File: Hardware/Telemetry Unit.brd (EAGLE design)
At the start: 50.8 x 82.5 mm, 56 parts, among them IC1 MEGA128-A, IC2 FT232RL, J2 503182-1852, J3 10118193-0001LF, Q1 10MHz, U1 MPL3115A2, U2 AOZ1280, U3 ICM-20649

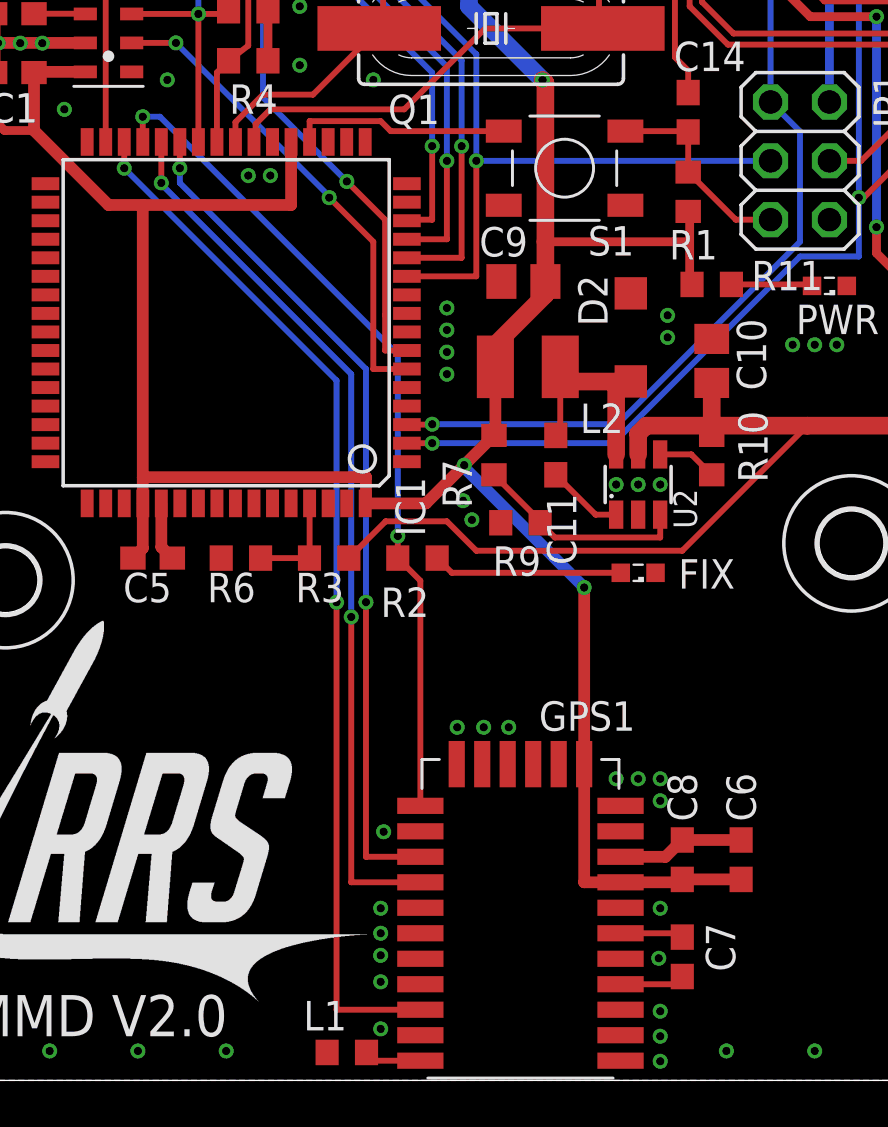
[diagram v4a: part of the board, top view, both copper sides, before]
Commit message: 0 Ohm Tuning Resistor
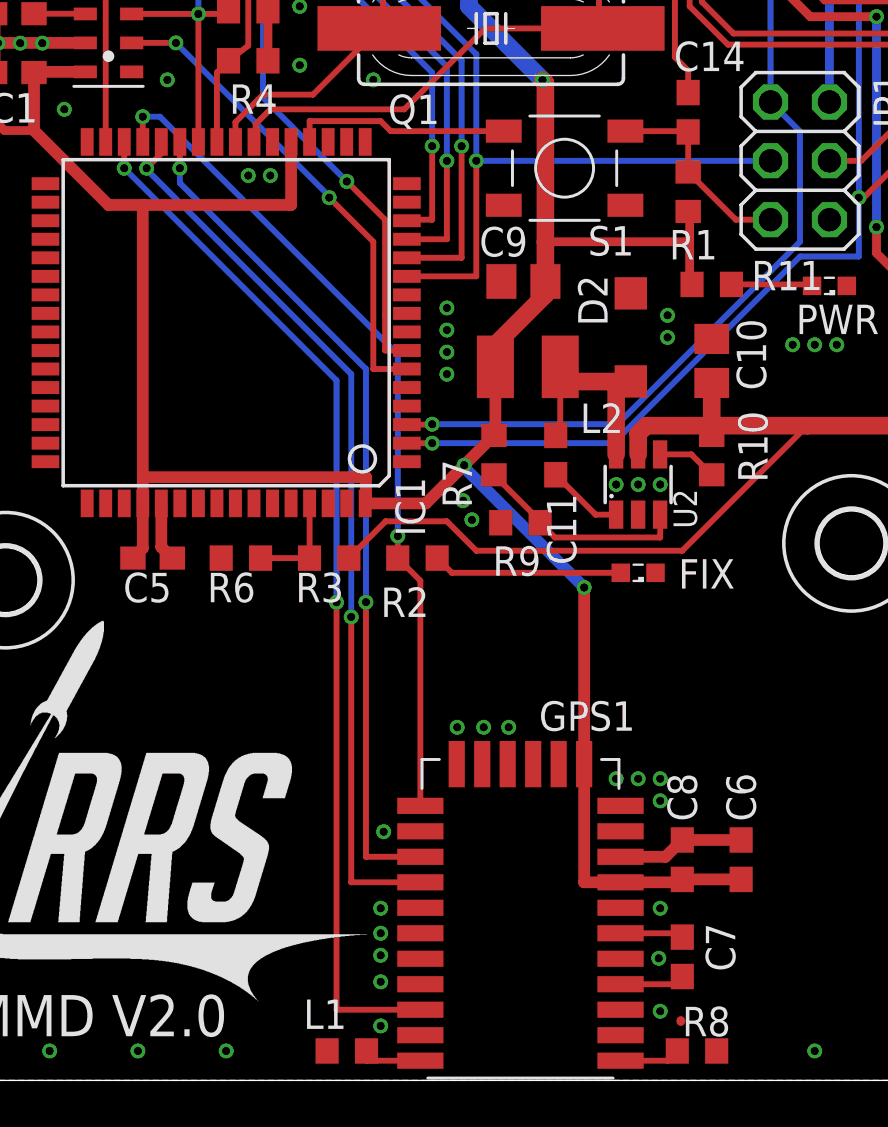
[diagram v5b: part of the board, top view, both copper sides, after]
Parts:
- added R8: 0, resistor:R0603
- moved L1 0.06 mm to (17.9, 1.27)
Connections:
- new net N$21: GPS1.1, R8.1
- net GND: now also R8.2; no longer GPS1.1
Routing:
- net N$21: track 0.00 -> 2.62 mm
- net TX1: track 38.3 -> 38.9 mm
- net GND: vias 81 -> 78
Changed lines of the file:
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@@
 <attribute name="VALUE" x="34.29" y="4.699" size="1.27" layer="27" rot="R90"/>
 </element>
-<element name="L1" library="TrackerPeripherals" package="L0603" value="1.8n" x="17.907" y="1.2065" smashed="yes" rot="R180">
-<attribute name="NAME" x="17.907" y="3.429" size="1.27" layer="25" rot="R180"/>
-<attribute name="VALUE" x="18.542" y="3.1115" size="1.27" layer="27" rot="R180"/>
+<element name="L1" library="TrackerPeripherals" package="L0603" value="1.8n" x="17.907" y="1.27" smashed="yes" rot="R180">
+<attribute name="NAME" x="17.907" y="3.4925" size="1.27" layer="25" rot="R180"/>
+<attribute name="VALUE" x="18.542" y="3.175" size="1.27" layer="27" rot="R180"/>
 </element>
 <element name="FIX" library="led" library_urn="urn:adsk.eagle:library:259" package="SML0603" package3d_urn="urn:adsk.eagle:package:15832/1" value="" x="30.48" y="21.9075" smashed="yes" rot="R180">
@@
 <attribute name="NAME" x="15.875" y="60.0075" size="1.27" layer="25" rot="R270"/>
 <attribute name="VALUE" x="13.0175" y="59.055" size="1.27" layer="27" rot="R270"/>
+</element>
+<element name="R8" library="resistor" library_urn="urn:adsk.eagle:library:348" package="R0603" package3d_urn="urn:adsk.eagle:package:23555/3" value="0" x="33.02" y="1.27" smashed="yes">
+<attribute name="NAME" x="32.385" y="1.905" size="1.27" layer="25"/>
+<attribute name="VALUE" x="32.385" y="-0.635" size="1.27" layer="27"/>
 </element>
 </elements>
@@
 <contactref element="IC2" pad="25"/>
 <contactref element="JP1" pad="6"/>
-<contactref element="GPS1" pad="1"/>
 <wire x1="10.375" y1="22.5425" x2="9.9" y2="23.0175" width="0.508" layer="1"/>
 <wire x1="9.9" y1="23.0175" x2="9.9" y2="24.9025" width="0.508" layer="1"/>
@@
 <vertex x="50.8" y="82.55"/>
 </polygon>
-<via x="31.4325" y="0.8255" extent="1-16" drill="0.35"/>
-<via x="31.4325" y="1.905" extent="1-16" drill="0.35"/>
 <via x="31.4325" y="2.9845" extent="1-16" drill="0.35"/>
 <via x="31.369" y="5.2705" extent="1-16" drill="0.35"/>
@@
 <via x="19.3675" y="6.35" extent="1-16" drill="0.35"/>
 <via x="19.3675" y="5.3975" extent="1-16" drill="0.35"/>
-<via x="19.3675" y="2.2225" extent="1-16" drill="0.35"/>
+<via x="19.3675" y="2.3495" extent="1-16" drill="0.35"/>
 <via x="19.3675" y="4.2545" extent="1-16" drill="0.35"/>
-<wire x1="31.4325" y1="0.85" x2="31.4325" y2="0.8255" width="0.381" layer="1"/>
-<wire x1="31.4325" y1="1.95" x2="31.4325" y2="1.905" width="0.381" layer="1"/>
+<wire x1="32.3215" y1="2.585" x2="32.3215" y2="2.54" width="0.381" layer="1"/>
 <wire x1="31.4325" y1="3.05" x2="31.4325" y2="2.9845" width="0.381" layer="1"/>
 <wire x1="31.4325" y1="7.449996875" x2="31.4325" y2="7.429503125" width="0.381" layer="1"/>
@@
 <via x="41.91" y="1.27" extent="1-16" drill="0.35"/>
 <via x="38.1" y="1.27" extent="1-16" drill="0.35"/>
-<via x="34.29" y="1.27" extent="1-16" drill="0.35"/>
 <via x="1.27" y="1.27" extent="1-16" drill="0.35"/>
 <via x="5.08" y="1.27" extent="1-16" drill="0.35"/>
@@
 <via x="5.715" y="41.91" extent="1-16" drill="0.35"/>
 <via x="19.05" y="43.18" extent="1-16" drill="0.35"/>
+<contactref element="R8" pad="2"/>
 </signal>
 <signal name="SDA">
@@
 <wire x1="18.0975" y1="8.55" x2="18.0975" y2="20.0025" width="0.254" layer="1"/>
 <via x="18.0975" y="20.0025" extent="1-16" drill="0.35"/>
-<wire x1="9.9" y1="40.5025" x2="9.9" y2="38.735" width="0.254" layer="1"/>
-<via x="9.9" y="38.735" extent="1-16" drill="0.35"/>
-<wire x1="9.9" y1="38.735" x2="9.9" y2="38.6775" width="0.254" layer="16"/>
-<wire x1="9.9" y1="38.6775" x2="18.0975" y2="30.48" width="0.254" layer="16"/>
+<wire x1="9.9" y1="40.5025" x2="9.9" y2="40.005" width="0.254" layer="1"/>
+<wire x1="9.9" y1="40.005" x2="9.265" y2="39.37" width="0.254" layer="1"/>
+<via x="9.265" y="39.37" extent="1-16" drill="0.35"/>
+<wire x1="9.265" y1="39.37" x2="9.265" y2="39.3125" width="0.254" layer="16"/>
+<wire x1="9.265" y1="39.3125" x2="18.0975" y2="30.48" width="0.254" layer="16"/>
 <wire x1="18.0975" y1="30.48" x2="18.0975" y2="20.0025" width="0.254" layer="16"/>
 </signal>
@@
 <contactref element="L1" pad="1"/>
 <wire x1="21.08" y1="0.85" x2="18.757" y2="0.85" width="0.254" layer="1"/>
-<wire x1="18.757" y1="0.85" x2="18.757" y2="1.2065" width="0.254" layer="1"/>
+<wire x1="18.757" y1="0.85" x2="18.757" y2="1.27" width="0.254" layer="1"/>
 </signal>
 <signal name="N$6">
@@
 <wire x1="14.9225" y1="59.255" x2="14.9225" y2="59.27" width="0.2032" layer="1"/>
 </signal>
+<signal name="N$21">
+<contactref element="GPS1" pad="1"/>
+<contactref element="R8" pad="1"/>
+<wire x1="29.72" y1="0.85" x2="31.75" y2="0.85" width="0.254" layer="1"/>
+<wire x1="31.75" y1="0.85" x2="32.17" y2="1.27" width="0.254" layer="1"/>
+</signal>
 </signals>

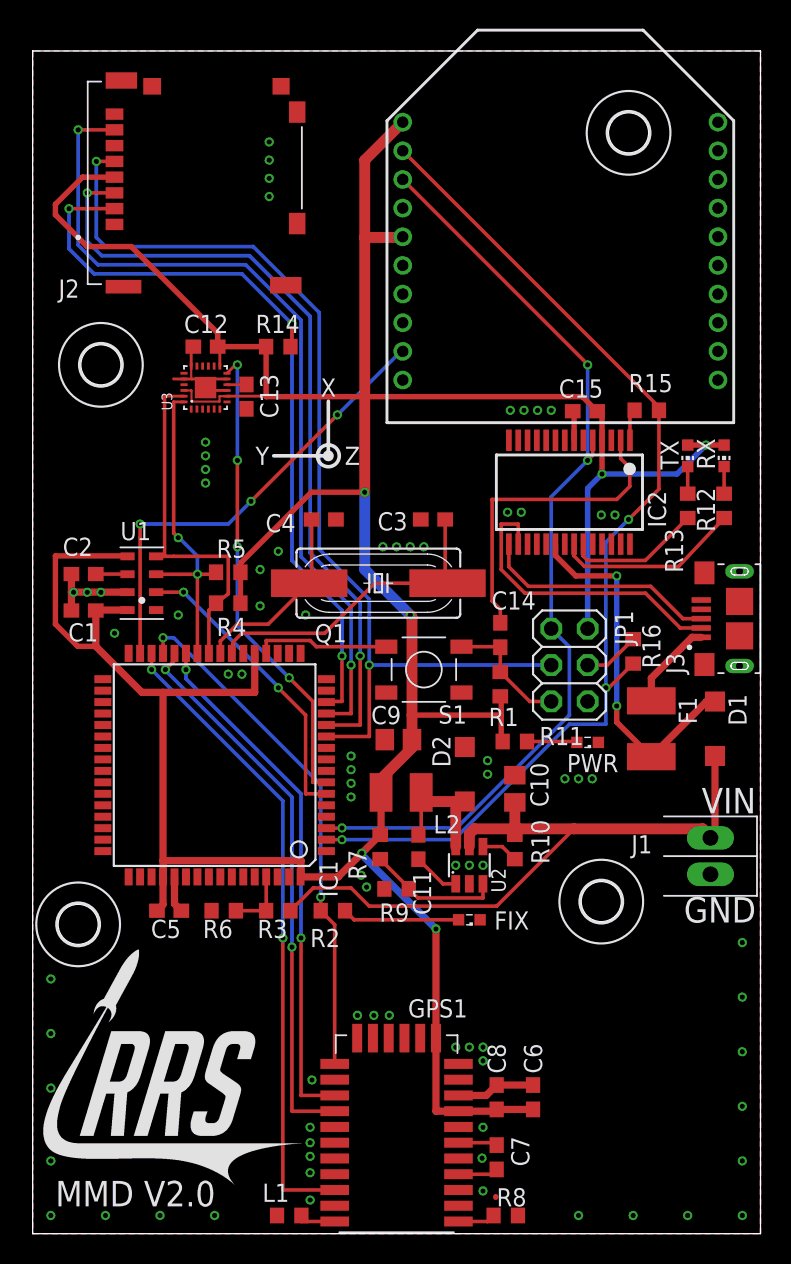
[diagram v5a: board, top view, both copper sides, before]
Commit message: Move GPS to long edge.  Much rerouting.  Shrunk board 0.25"
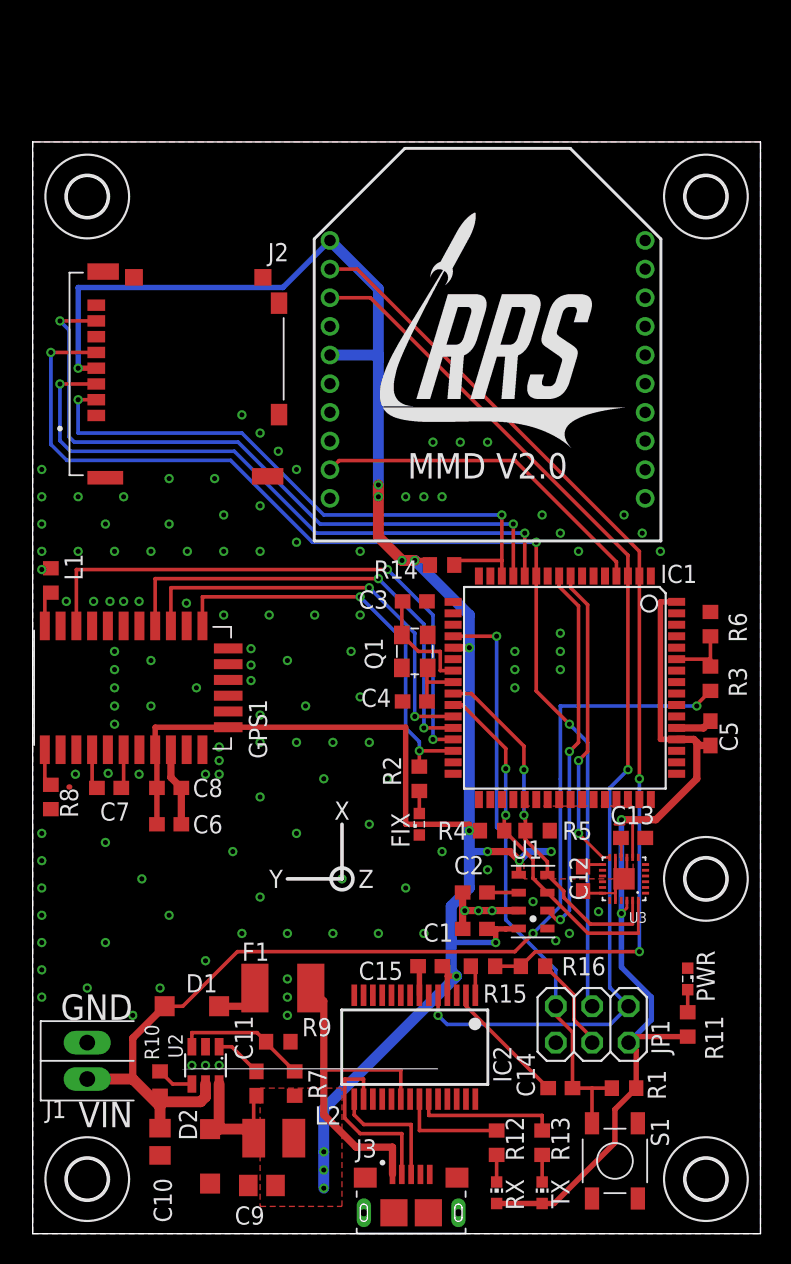
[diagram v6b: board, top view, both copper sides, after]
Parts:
- added U$5: (no value), holes:2,8
- Q1: device crystal:HC49UP -> crystal-geyer_V1_0:3.2X2.5_KX-7
- moved U$3 82.2 mm to (3.81, 3.81)
- moved U$2 60.9 mm to (3.81, 72.4)
- moved RX 53.8 mm to (32.4, 2.86), turned to 0 degrees
- moved TX 52.4 mm to (35.6, 2.86), turned to 0 degrees
- moved J3 47.4 mm to (26.4, 1.46), turned to 0 degrees
- moved L1 47.3 mm to (1.27, 45.6), turned to 90 degrees
- moved U$4 47.3 mm to (47.0, 3.81)
- moved R12 47.2 mm to (32.4, 6.35), turned to 90 degrees
- moved J1 45.8 mm to (3.81, 12.1), turned to 180 degrees
- moved R13 45.6 mm to (35.6, 6.35), turned to 90 degrees
- moved C12 45.5 mm to (38.4, 24.8), turned to 270 degrees
- moved U3 45.0 mm to (41.3, 24.8), turned to 180 degrees
- moved U$1 43.8 mm to (47.0, 72.4), turned to 0 degrees
- moved R8 43.1 mm to (1.27, 30.5), turned to 270 degrees
- moved D1 41.3 mm to (11.1, 15.9), turned to 0 degrees
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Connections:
- removed net N$22: F1.1, J3.1
- new net 5V_USB: F1.1, IC2.20, J3.1
- net !GPS_SLP: now also IC1.29; no longer IC1.30
- net ACCEL_INT: now also IC1.8; no longer IC1.7
- net ALT_INT: now also IC1.9; no longer IC1.6
- net FIX: now also IC1.30; no longer IC1.29
- net N$5: now also IC1.59; no longer IC1.61
- net RF_SLP: now also IC1.4; no longer IC1.31
- net V_USB: no longer IC2.20
- net XTAL2: now also Q1.3; no longer Q1.2
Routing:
- net +3V3: track 258.3 -> 231.1 mm, vias 6 -> 17
- net 5V_USB: track 0.00 -> 24.3 mm
- net VBAT: track 49.7 -> 73.8 mm, vias 0 -> 2
- net !RST: track 18.3 -> 42.0 mm, vias 0 -> 1
- net V_USB: track 25.3 -> 3.77 mm, vias 2 -> 0
- net XTAL2: track 22.0 -> 7.76 mm
- net N$16: track 22.3 -> 8.86 mm
- net ACCEL_INT: track 33.2 -> 21.6 mm, vias 4 -> 2
- net CS_SD: track 54.3 -> 43.3 mm, vias 3 -> 2
- net MISO: track 58.9 -> 48.0 mm
- net MOSI: track 55.3 -> 44.6 mm
- net TX0/PDO: track 66.1 -> 76.3 mm, vias 3 -> 2
- net SCK: track 71.0 -> 80.3 mm, vias 2 -> 3
- net XTAL1: track 13.2 -> 4.22 mm
- net N$11: track 21.4 -> 12.7 mm
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- added copper zone on layer 1, net +3V3
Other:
- board size 50.8 x 82.5 mm -> 50.8 x 76.2 mm

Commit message: Update EAGLE and improve silkscreen
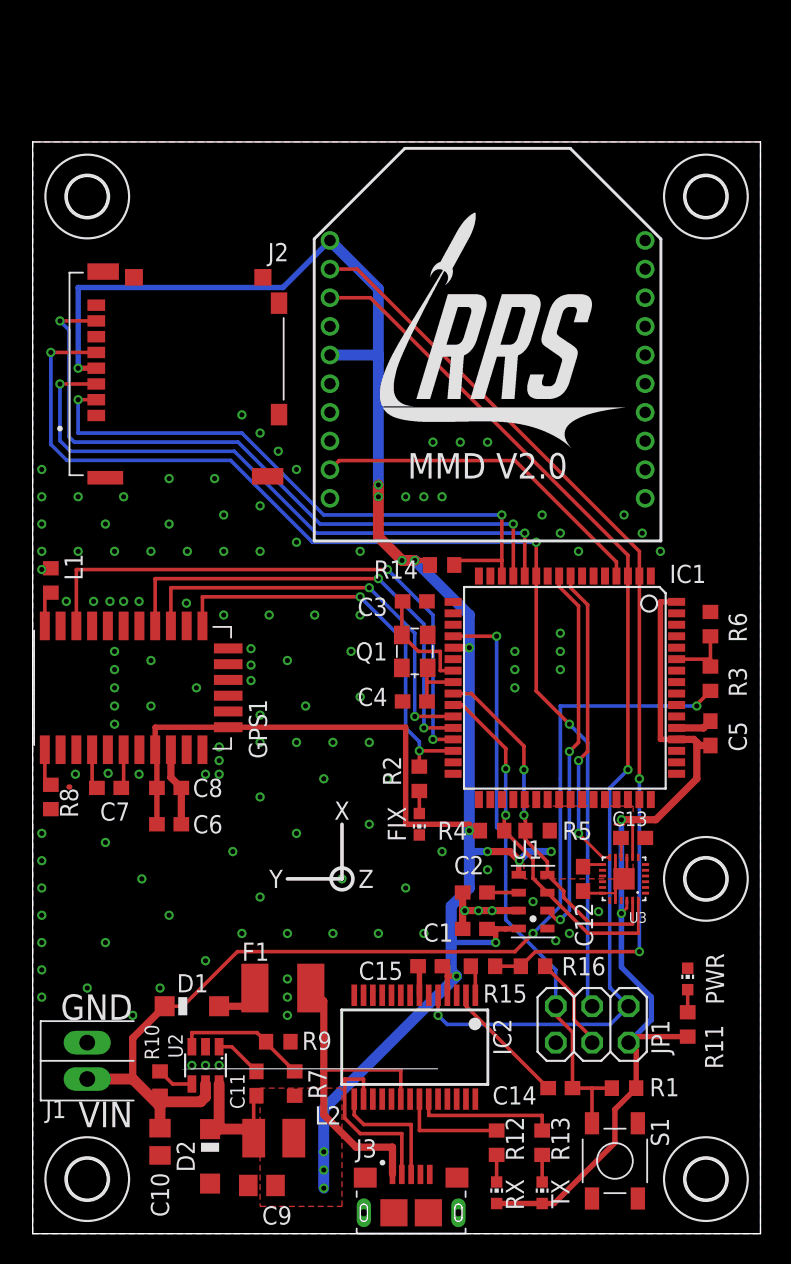
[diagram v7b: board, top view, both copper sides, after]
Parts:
- FIX, PWR: device led:SML0603 -> led:CHIP-LED0603
- turned FIX to 180 degrees
- turned PWR to 0 degrees

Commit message: Stitching vias for rest of board
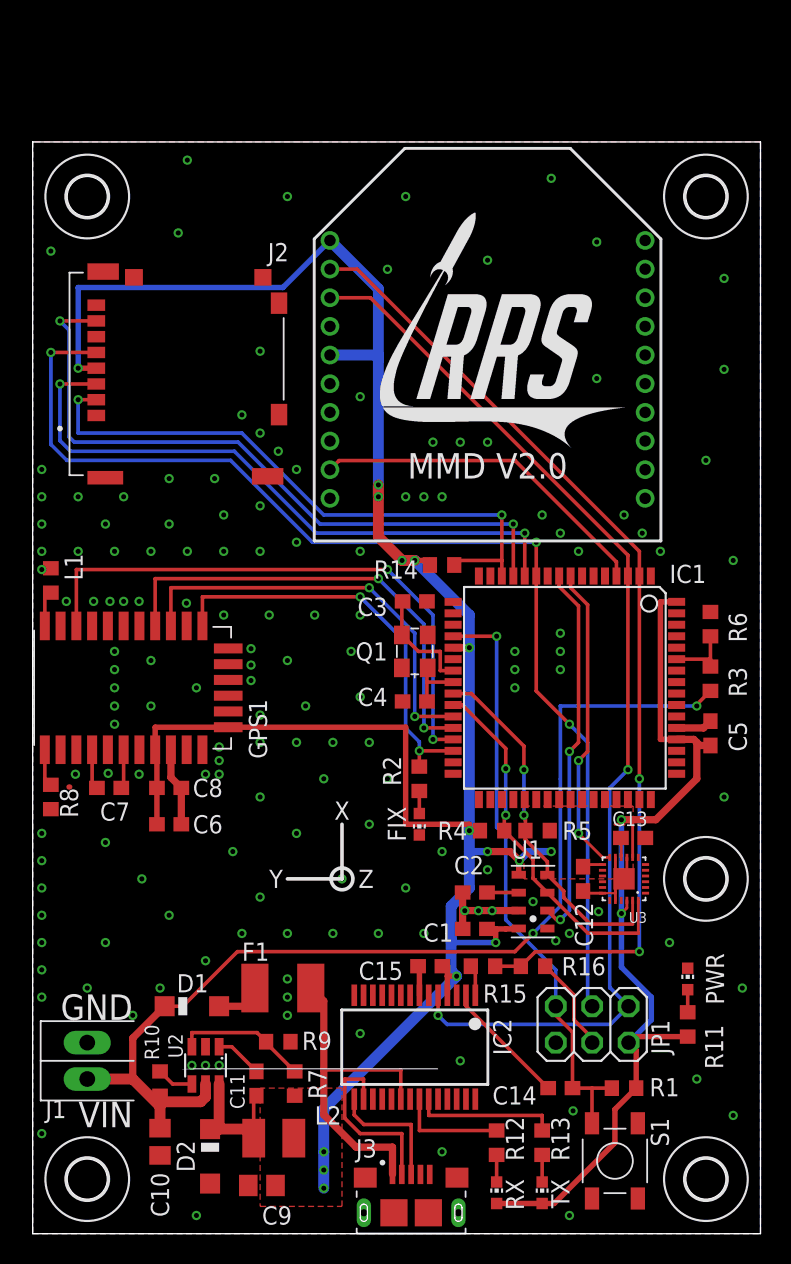
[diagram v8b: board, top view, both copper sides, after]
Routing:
- net GND: vias 124 -> 152
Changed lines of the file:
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@@
 <drawing>
 <settings>
-<setting alwaysvectorfont="yes"/>
+<setting alwaysvectorfont="no"/>
 <setting verticaltext="up"/>
 </settings>
@@
 <layer number="49" name="Reference" color="7" fill="1" visible="no" active="yes"/>
 <layer number="50" name="dxf" color="7" fill="1" visible="no" active="no"/>
-<layer number="51" name="tDocu" color="7" fill="1" visible="no" active="yes"/>
+<layer number="51" name="tDocu" color="7" fill="1" visible="yes" active="yes"/>
 <layer number="52" name="bDocu" color="7" fill="1" visible="no" active="yes"/>
 <layer number="53" name="tGND_GNDA" color="7" fill="1" visible="no" active="no"/>
@@
 <via x="24.765" y="31.75" extent="1-16" drill="0.35"/>
 <via x="28.575" y="26.67" extent="1-16" drill="0.35"/>
+<via x="22.86" y="13.97" extent="1-16" drill="0.35"/>
+<via x="29.845" y="12.065" extent="1-16" drill="0.35"/>
+<via x="28.575" y="5.715" extent="1-16" drill="0.35"/>
+<via x="46.355" y="10.795" extent="1-16" drill="0.35"/>
+<via x="48.895" y="8.255" extent="1-16" drill="0.35"/>
+<via x="49.53" y="17.145" extent="1-16" drill="0.35"/>
+<via x="44.45" y="20.32" extent="1-16" drill="0.35"/>
+<via x="48.26" y="30.48" extent="1-16" drill="0.35"/>
+<via x="48.895" y="46.99" extent="1-16" drill="0.35"/>
+<via x="46.99" y="53.975" extent="1-16" drill="0.35"/>
+<via x="48.26" y="60.325" extent="1-16" drill="0.35"/>
+<via x="39.37" y="69.215" extent="1-16" drill="0.35"/>
+<via x="31.75" y="67.945" extent="1-16" drill="0.35"/>
+<via x="26.035" y="72.39" extent="1-16" drill="0.35"/>
+<via x="10.795" y="74.93" extent="1-16" drill="0.35"/>
+<via x="10.16" y="69.85" extent="1-16" drill="0.35"/>
+<via x="17.78" y="72.39" extent="1-16" drill="0.35"/>
+<via x="36.195" y="73.66" extent="1-16" drill="0.35"/>
+<via x="39.37" y="59.69" extent="1-16" drill="0.35"/>
+<via x="24.765" y="67.31" extent="1-16" drill="0.35"/>
+<via x="22.86" y="58.42" extent="1-16" drill="0.35"/>
+<via x="15.875" y="61.595" extent="1-16" drill="0.35"/>
+<via x="48.26" y="66.675" extent="1-16" drill="0.35"/>
+<via x="1.27" y="68.58" extent="1-16" drill="0.35"/>
+<via x="11.43" y="1.27" extent="1-16" drill="0.35"/>
+<via x="37.719" y="8.5725" extent="1-16" drill="0.35"/>
+<via x="37.465" y="1.27" extent="1-16" drill="0.35"/>
+<via x="0.635" y="6.985" extent="1-16" drill="0.35"/>
 </signal>
 <signal name="SDA">
